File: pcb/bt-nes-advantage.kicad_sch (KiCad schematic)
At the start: 18 parts, among them J1 USB_C_Receptacle_PowerOnly_6P, J2 Screw_Terminal_01x02, J3 Conn_01x08, U1 ESP32-C3_SUPERMINI_TH, U2 HW775

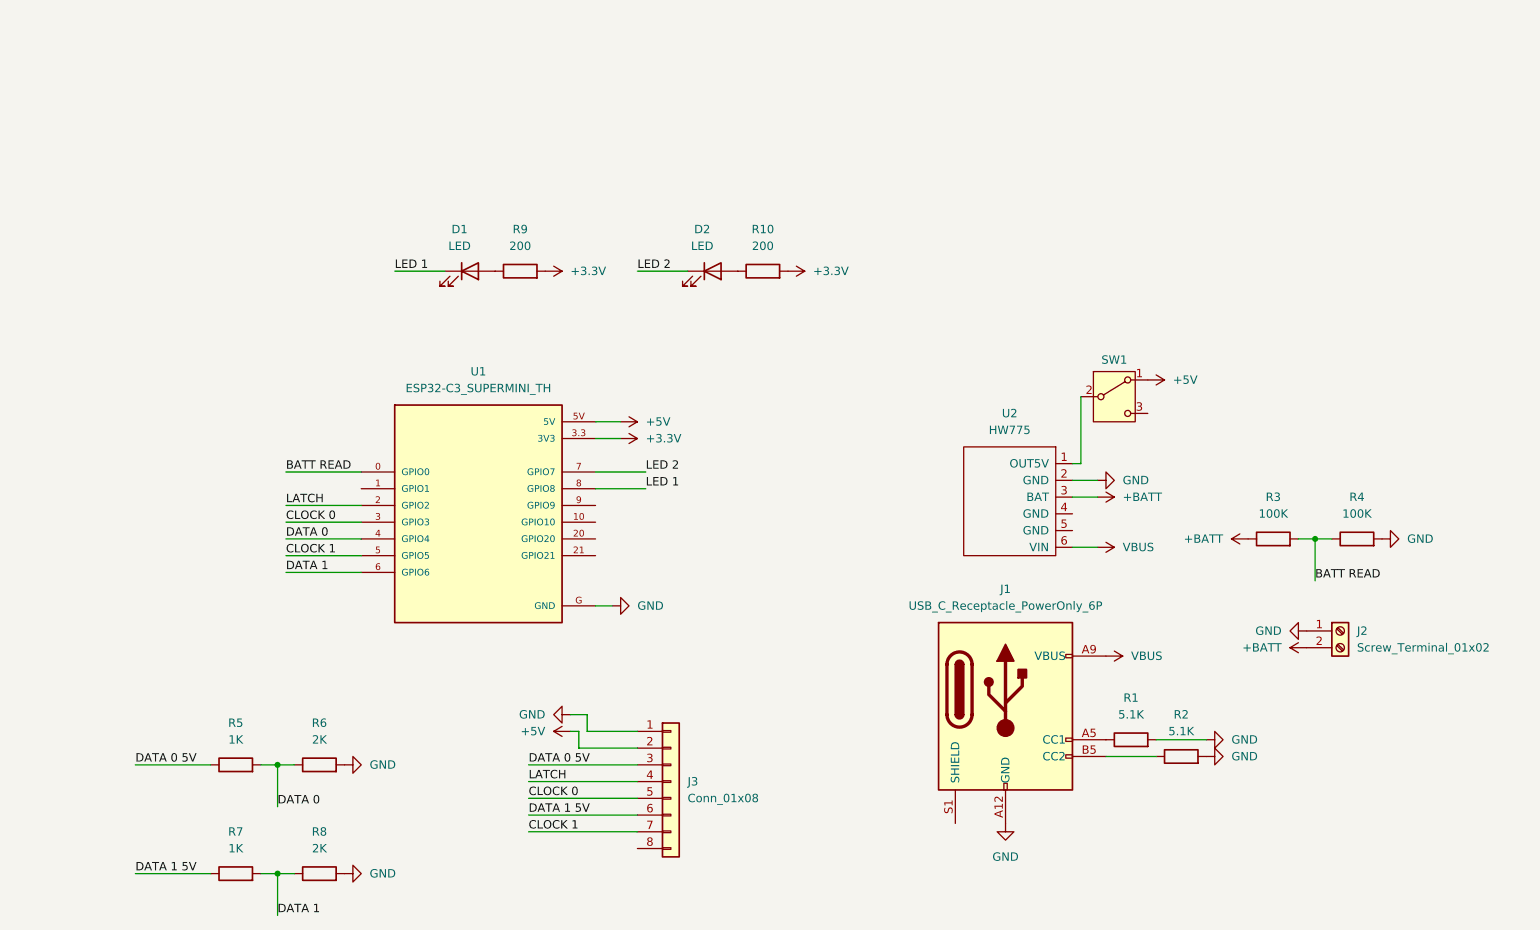
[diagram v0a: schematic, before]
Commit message: New PCB revision. Updated firmware logic.
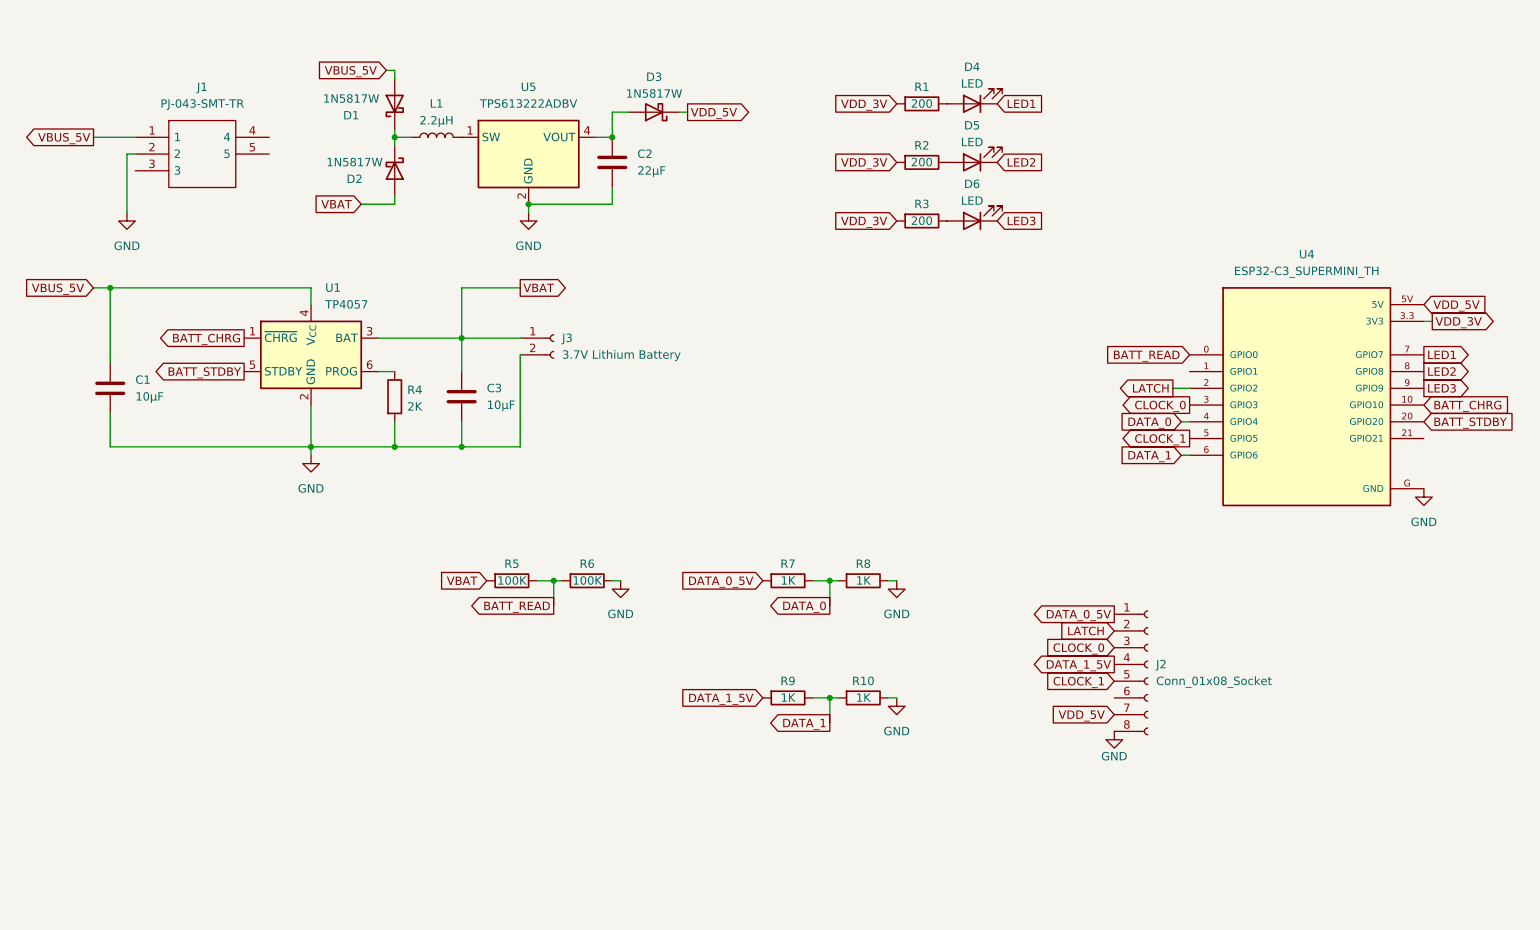
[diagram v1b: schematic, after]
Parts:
- removed D1, D2: LED, LED_SMD:LED_0201_0603Metric_Pad0.64x0.40mm_HandSolder, symbol Device:LED
- removed J1: USB_C_Receptacle_PowerOnly_6P, Connector_USB:USB_C_Receptacle_GCT_USB4125-xx-x-0190_6P_TopMnt_Horizontal, symbol Connector:USB_C_Receptacle_PowerOnly_6P
- removed J2: Screw_Terminal_01x02, TerminalBlock_Phoenix:TerminalBlock_Phoenix_PT-1,5-2-5.0-H_1x02_P5.00mm_Horizontal, symbol Connector:Screw_Terminal_01x02
- removed J3: Conn_01x08, Connector_PinHeader_2.54mm:PinHeader_1x08_P2.54mm_Horizontal, symbol Connector_Generic:Conn_01x08
- removed SW1: ~, Button_Switch_THT:SW_Slide_SPDT_Angled_CK_OS102011MA1Q, symbol Switch:SW_SPDT
- removed U1: ESP32-C3_SUPERMINI_TH, bt-nes-advantage:MODULE_ESP32-C3_SUPERMINI, symbol bt-nes-advantage:ESP32-C3_SUPERMINI_TH
- removed U2: HW775, bt-nes-advantage:Charger2A, symbol bt-nes-advantage:HW775
- added C1, C3: 10µF, Capacitor_SMD:C_0603_1608Metric_Pad1.08x0.95mm_HandSolder, symbol Device:C
- added C2: 22µF, Capacitor_SMD:C_0603_1608Metric_Pad1.08x0.95mm_HandSolder, symbol Device:C
- added D1, D2, D3: 1N5817W, Diode_SMD:D_SOD-123, symbol Device:D_Schottky
- added D4, D5, D6: LED, LED_SMD:LED_0603_1608Metric_Pad1.05x0.95mm_HandSolder, symbol Device:LED
- added J1: PJ-043-SMT-TR, My_Library:PJ043SMTTR, symbol My_Library:PJ-043-SMT-TR
- added J2: Conn_01x08_Socket, Connector_JST:JST_XH_S8B-XH-A_1x08_P2.50mm_Horizontal, symbol Connector:Conn_01x08_Socket
- added J3: 3.7V Lithium Battery, Connector_JST:JST_PH_S2B-PH-K_1x02_P2.00mm_Horizontal, symbol Connector:Conn_01x02_Socket
- added L1: 2.2µH, Inductor_SMD:L_1008_2520Metric_Pad1.43x2.20mm_HandSolder, symbol Device:L
- added U1: TP4057, Package_TO_SOT_SMD:TSOT-23-6, symbol Battery_Management:TP4057
- added U4: ESP32-C3_SUPERMINI_TH, My_Library:MODULE_ESP32-C3_SUPERMINI, symbol My_Library:ESP32-C3_SUPERMINI_TH
- added U5: TPS613222ADBV, Package_TO_SOT_SMD:SOT-23-5, symbol Regulator_Switching:TPS613222ADBV
- R1, R2: value 5.1K -> 200; footprint Resistor_SMD:R_0201_0603Metric_Pad0.64x0.40mm_HandSolder -> Resistor_SMD:R_0603_1608Metric_Pad0.98x0.95mm_HandSolder
- R10, R9: value 200 -> 1K; footprint Resistor_SMD:R_0201_0603Metric_Pad0.64x0.40mm_HandSolder -> Resistor_SMD:R_0603_1608Metric_Pad0.98x0.95mm_HandSolder
- R3: value 100K -> 200; footprint Resistor_SMD:R_0201_0603Metric_Pad0.64x0.40mm_HandSolder -> Resistor_SMD:R_0603_1608Metric_Pad0.98x0.95mm_HandSolder
- R4: value 100K -> 2K; footprint Resistor_SMD:R_0201_0603Metric_Pad0.64x0.40mm_HandSolder -> Resistor_SMD:R_0603_1608Metric_Pad0.98x0.95mm_HandSolder
- R5: value 1K -> 100K; footprint Resistor_SMD:R_0201_0603Metric_Pad0.64x0.40mm_HandSolder -> Resistor_SMD:R_0603_1608Metric_Pad0.98x0.95mm_HandSolder
- R6: value 2K -> 100K; footprint Resistor_SMD:R_0201_0603Metric_Pad0.64x0.40mm_HandSolder -> Resistor_SMD:R_0603_1608Metric_Pad0.98x0.95mm_HandSolder
- R7: footprint Resistor_SMD:R_0201_0603Metric_Pad0.64x0.40mm_HandSolder -> Resistor_SMD:R_0603_1608Metric_Pad0.98x0.95mm_HandSolder
- R8: value 2K -> 1K; footprint Resistor_SMD:R_0201_0603Metric_Pad0.64x0.40mm_HandSolder -> Resistor_SMD:R_0603_1608Metric_Pad0.98x0.95mm_HandSolder
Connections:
- net GND: now also R10.1, R6.1, R8.1, C1.2, C2.2, C3.2, J1.2, J2.8 (Pin_8), J3.2 (Pin_2), U1.2 (GND), U4.G (GND), U5.2 (GND); no longer R1.2, R2.2, R6.2, R8.2
- net LATCH: now also J2.2 (Pin_2), U4.2 (GPIO2)
- net at R1.1: now also D4.2 (A)
- net at R2.1: now also D5.2 (A)
- net DATA_1: now reaches R9.1
- net DATA_1: now also R10.2, U4.6 (GPIO6)
- net +3.3V renamed DATA_1_5V
- net DATA_1_5V: now also J2.4 (Pin_4); no longer R10.2
- net +BATT: no longer names the net of R3.1
- net +BATT: now also D6.2 (A)
- net BATT READ: no longer names the net of R4.1
- net BATT READ: now also U1.6 (PROG); no longer R3.2
- net DATA 0 renamed VBAT
- net VBAT: now also C3.1, D2.2 (A), J3.1 (Pin_1), U1.3 (BAT); no longer R6.1
- net DATA 0 5V renamed BATT_READ
- net BATT_READ: now also R6.2, U4.0 (GPIO0)
- net DATA 1 renamed DATA_0_5V
- net DATA_0_5V: now also J2.1 (Pin_1); no longer R8.1
- net DATA 1 5V renamed DATA_0
- net DATA_0: now also R8.2, U4.4 (GPIO4)
- new net: C2.1, D3.2 (A), U5.4 (VOUT)
- new net: D1.1 (K), D2.1 (K), L1.1
- new net: L1.2, U5.1 (SW)
- new net BATT_CHRG: U1.1 (~{CHRG}), U4.10 (GPIO10)
- new net BATT_STDBY: U1.5 (STDBY), U4.20 (GPIO20)
- new net CLOCK_0: J2.3 (Pin_3), U4.3 (GPIO3)
- new net CLOCK_1: J2.5 (Pin_5), U4.5 (GPIO5)
- new net LED1: D4.1 (K), U4.7 (GPIO7)
- new net LED2: D5.1 (K), U4.8 (GPIO8)
- new net LED3: D6.1 (K), U4.9 (GPIO9)
- new net VBUS_5V: C1.1, D1.2 (A), J1.1, U1.4 (V_{CC})
- new net VDD_3V: R1.2, R2.2, R3.2, U4.3.3 (3V3)
- new net VDD_5V: D3.1 (K), J2.7 (Pin_7), U4.5V

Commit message: pcb update
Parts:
- J1: footprint My_Library:PJ043SMTTR -> My_Library:CUI_PJ-040-SMT-TR; symbol My_Library:PJ-043-SMT-TR -> My_Library:PJ-040-SMT-TR; MANUFACTURER (none) -> CUI Devices; MAXIMUM_PACKAGE_HEIGHT (none) -> 3.00mm; PARTREV (none) -> 1.07; STANDARD (none) -> Manufacturer Recommendations
- renumbered U5 to U2, U4 to U3
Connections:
- net GND: now also J1.3
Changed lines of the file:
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@@
+	)
+	(junction
+		(at 36.83 35.56)
+		(diameter 0)
+		(color 0 0 0 0)
 	)
 	(junction
@@
 	(wire
 		(pts
-			(xy 34.29 33.02) (xy 40.64 33.02)
-		)
-		(stroke
-			(width 0)
-			(type default)
-		)
-	)
-	(wire
-		(pts
 			(xy 67.31 55.88) (xy 67.31 58.42)
 		)
@@
 	(wire
 		(pts
-			(xy 40.64 35.56) (xy 39.37 35.56)
-		)
-		(stroke
-			(width 0)
-			(type default)
-		)
-	)
-	(wire
-		(pts
 			(xy 80.01 33.02) (xy 82.55 33.02)
 		)
@@
 	(wire
 		(pts
-			(xy 39.37 35.56) (xy 39.37 44.45)
-		)
-		(stroke
-			(width 0)
-			(type default)
-		)
-	)
-	(wire
-		(pts
 			(xy 36.83 80.01) (xy 67.31 80.01)
 		)
@@
 		(pts
 			(xy 90.17 76.2) (xy 90.17 80.01)
+		)
+		(stroke
+			(width 0)
+			(type default)
+		)
+	)
+	(wire
+		(pts
+			(xy 36.83 35.56) (xy 41.91 35.56)
 		)
 		(stroke
@@
 	(global_label "VBUS_5V"
 		(shape output)
-		(at 34.29 33.02 180)
-		(fields_autoplaced yes)
-		(effects
-			(font
-				(size 1.27 1.27)
-			)
-			(justify right)
-		)
-		(property "Intersheetrefs" "${INTERSHEET_REFS}"
-			(at 23.1405 33.02 0)
-			(effects
-				(font
-					(size 1.27 1.27)
-				)
-				(justify right)
+		(at 44.45 35.56 0)
+		(fields_autoplaced yes)
+		(effects
+			(font
+				(size 1.27 1.27)
+			)
+			(justify left)
+		)
+		(property "Intersheetrefs" "${INTERSHEET_REFS}"
+			(at 55.5995 35.56 0)
+			(effects
+				(font
+					(size 1.27 1.27)
+				)
+				(justify left)
 				(hide yes)
 			)
@@
 	)
 	(symbol
-		(lib_id "My_Library:PJ-043-SMT-TR")
-		(at 40.64 33.02 0)
+		(lib_id "My_Library:PJ-040-SMT-TR")
+		(at 41.91 25.4 270)
 		(unit 1)
 		(exclude_from_sim no)
@@
 		(on_board yes)
 		(dnp no)
-		(fields_autoplaced yes)
 		(property "Reference" "J1"
-			(at 50.8 25.4 0)
-			(effects
-				(font
-					(size 1.27 1.27)
-				)
+			(at 33.02 15.494 90)
+			(effects
+				(font
+					(size 1.27 1.27)
+				)
+				(justify left)
 			)
 		)
 		(property "Value" "PJ-043-SMT-TR"
-			(at 50.8 27.94 0)
-			(effects
-				(font
-					(size 1.27 1.27)
-				)
-			)
-		)
-		(property "Footprint" "My_Library:PJ043SMTTR"
-			(at 57.15 30.48 0)
-			(effects
-				(font
-					(size 1.27 1.27)
-				)
-				(justify left)
-				(hide yes)
-			)
-		)
-		(property "Datasheet" "https://www.sameskydevices.com/product/resource/supplyframepdf/pj-043-smt-tr.pdf"
-			(at 57.15 33.02 0)
-			(effects
-				(font
-					(size 1.27 1.27)
-				)
-				(justify left)
+			(at 33.02 18.034 90)
+			(effects
+				(font
+					(size 1.27 1.27)
+				)
+				(justify left)
+			)
+		)
+		(property "Footprint" "My_Library:CUI_PJ-040-SMT-TR"
+			(at 41.91 25.4 0)
+			(effects
+				(font
+					(size 1.27 1.27)
+				)
+				(justify bottom)
+				(hide yes)
+			)
+		)
+		(property "Datasheet" "https://www.sameskydevices.com/product/resource/pj-040-smt-tr.pdf"
+			(at 41.91 25.4 0)
+			(effects
+				(font
+					(size 1.27 1.27)
+				)
 				(hide yes)
 			)
 		)
 		(property "Description" "1.0 x 3.2 mm, 2.0 A, Horizontal, Surface Mount (SMT), Shielded, Dc Power Jack Connector"
-			(at 40.64 33.02 0)
+			(at 41.91 25.4 0)
 			(effects
 				(font
@@
 		)
 		(property "Description_1" "1.0 x 3.2 mm, 2.0 A, Horizontal, Surface Mount (SMT), Shielded, Dc Power Jack Connector"
-			(at 57.15 35.56 0)
+			(at 39.37 41.91 0)
 			(effects
 				(font
@@
 		)
 		(property "Height" "4.77"
-			(at 57.15 38.1 0)
+			(at 36.83 41.91 0)
 			(effects
 				(font
@@
 		)
 		(property "Mouser Part Number" "490-PJ-043-SMT-TR"
-			(at 57.15 40.64 0)
+			(at 34.29 41.91 0)
 			(effects
 				(font
@@
 		)
 		(property "Mouser Price/Stock" "https://www.mouser.co.uk/ProductDetail/Same-Sky/PJ-043-SMT-TR?qs=WyjlAZoYn504fsXktSvOWQ%3D%3D"
-			(at 57.15 43.18 0)
+			(at 31.75 41.91 0)
 			(effects
 				(font
@@
 		)
 		(property "Manufacturer_Name" "Same Sky"
-			(at 57.15 45.72 0)
+			(at 29.21 41.91 0)
 			(effects
 				(font
@@
 		)
 		(property "Manufacturer_Part_Number" "PJ-043-SMT-TR"
-			(at 57.15 48.26 0)
-			(effects
-				(font
-					(size 1.27 1.27)
-				)
-				(justify left)
+			(at 26.67 41.91 0)
+			(effects
+				(font
+					(size 1.27 1.27)
+				)
+				(justify left)
+				(hide yes)
+			)
+		)
+		(property "PARTREV" "1.07"
+			(at 41.91 25.4 0)
+			(effects
+				(font
+					(size 1.27 1.27)
+				)
+				(justify bottom)
+				(hide yes)
+			)
+		)
+		(property "STANDARD" "Manufacturer Recommendations"
+			(at 41.91 25.4 0)
+			(effects
+				(font
+					(size 1.27 1.27)
+				)
+				(justify bottom)
+				(hide yes)
+			)
+		)
+		(property "MAXIMUM_PACKAGE_HEIGHT" "3.00mm"
+			(at 41.91 25.4 0)
+			(effects
+				(font
+					(size 1.27 1.27)
+				)
+				(justify bottom)
+				(hide yes)
+			)
+		)
+		(property "MANUFACTURER" "CUI Devices"
+			(at 41.91 25.4 0)
+			(effects
+				(font
+					(size 1.27 1.27)
+				)
+				(justify bottom)
 				(hide yes)
 			)
 		)
 		(pin "3"
-		)
-		(pin "4"
-		)
-		(pin "5"
 		)
 		(pin "2"
@@
 		(dnp no)
 		(fields_autoplaced yes)
-		(property "Reference" "U4"
+		(property "Reference" "U3"
 			(at 218.44 50.8 0)
 			(effects
@@
 			(project ""
 				(path "/65a65c21-f7b5-417f-8913-03f557b05873"
-					(reference "U4")
+					(reference "U3")
 					(unit 1)
 				)
@@
 		(dnp no)
 		(fields_autoplaced yes)
-		(property "Reference" "U5"
+		(property "Reference" "U2"
 			(at 100.33 25.4 0)
 			(effects
@@
 			(project ""
 				(path "/65a65c21-f7b5-417f-8913-03f557b05873"
-					(reference "U5")
+					(reference "U2")
 					(unit 1)
 				)
@@
 	(symbol
 		(lib_id "power:GND")
-		(at 39.37 44.45 0)
+		(at 36.83 35.56 0)
 		(unit 1)
 		(exclude_from_sim no)
@@
 		(fields_autoplaced yes)
 		(property "Reference" "#PWR07"
-			(at 39.37 50.8 0)
+			(at 36.83 41.91 0)
 			(effects
 				(font
@@
 		)
 		(property "Value" "GND"
-			(at 39.37 49.53 0)
+			(at 36.83 40.64 0)
 			(effects
 				(font
@@
 		)
 		(property "Footprint" ""
-			(at 39.37 44.45 0)
+			(at 36.83 35.56 0)
 			(effects
 				(font
@@
 		)
 		(property "Datasheet" ""
-			(at 39.37 44.45 0)
+			(at 36.83 35.56 0)
 			(effects
 				(font
@@
 		)
 		(property "Description" "Power symbol creates a global label with name \"GND\" , ground"
-			(at 39.37 44.45 0)
-			(effects
-				(font
+			(at 36.83 35.56 0)
+			(effects
+				(font

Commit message: Add NESController class for handling NES controller input
- Implemented NESController class with methods for reading button states, checking state changes, and managing player selection.
- Added support for two players with separate button states and selection callbacks.
- Included methods to retrieve button states, axis values, and hat direction.
- Initialized controller pins and set up input handling in the constructor and begin method.
- Implemented debouncing for player selection changes.
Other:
- company: (none) -> Cajun Panda's Retro Gaming
- title: (none) -> Bluetooth NES Advantage
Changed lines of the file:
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@@
 	(generator_version "9.0")
 	(paper "A4")
+	(title_block
+		(title "Bluetooth NES Advantage")
+		(date "2025-06-20")
+		(rev "1.0")
+		(company "Cajun Panda's Retro Gaming")
+	)
 	(junction
 		(at 67.31 80.01)
